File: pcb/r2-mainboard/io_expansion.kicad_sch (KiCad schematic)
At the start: 6 parts, among them J22 HC-FPC-05-09-6RLTAG, J23 HC-FPC-05-09-6RLTAG, U54 TPS22914BYFPR, U55 TPS22914BYFPR

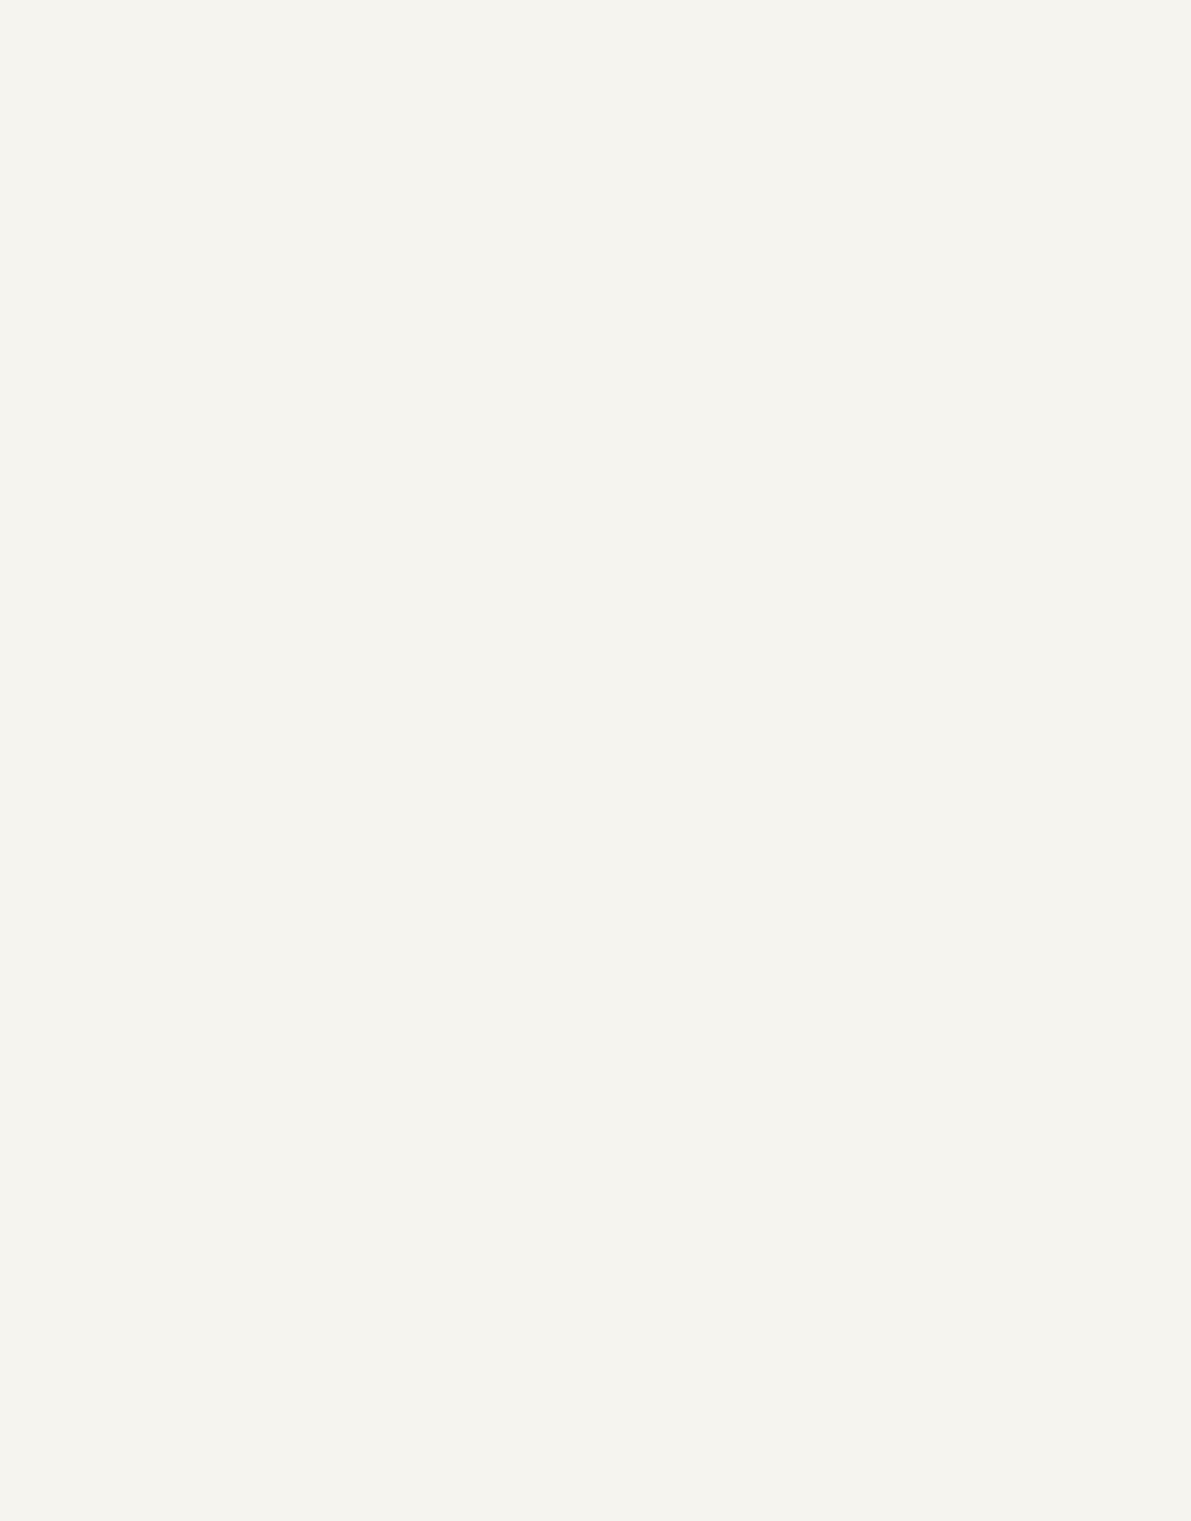
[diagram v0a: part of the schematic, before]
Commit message: change layout and reduce board size + add second usb host only
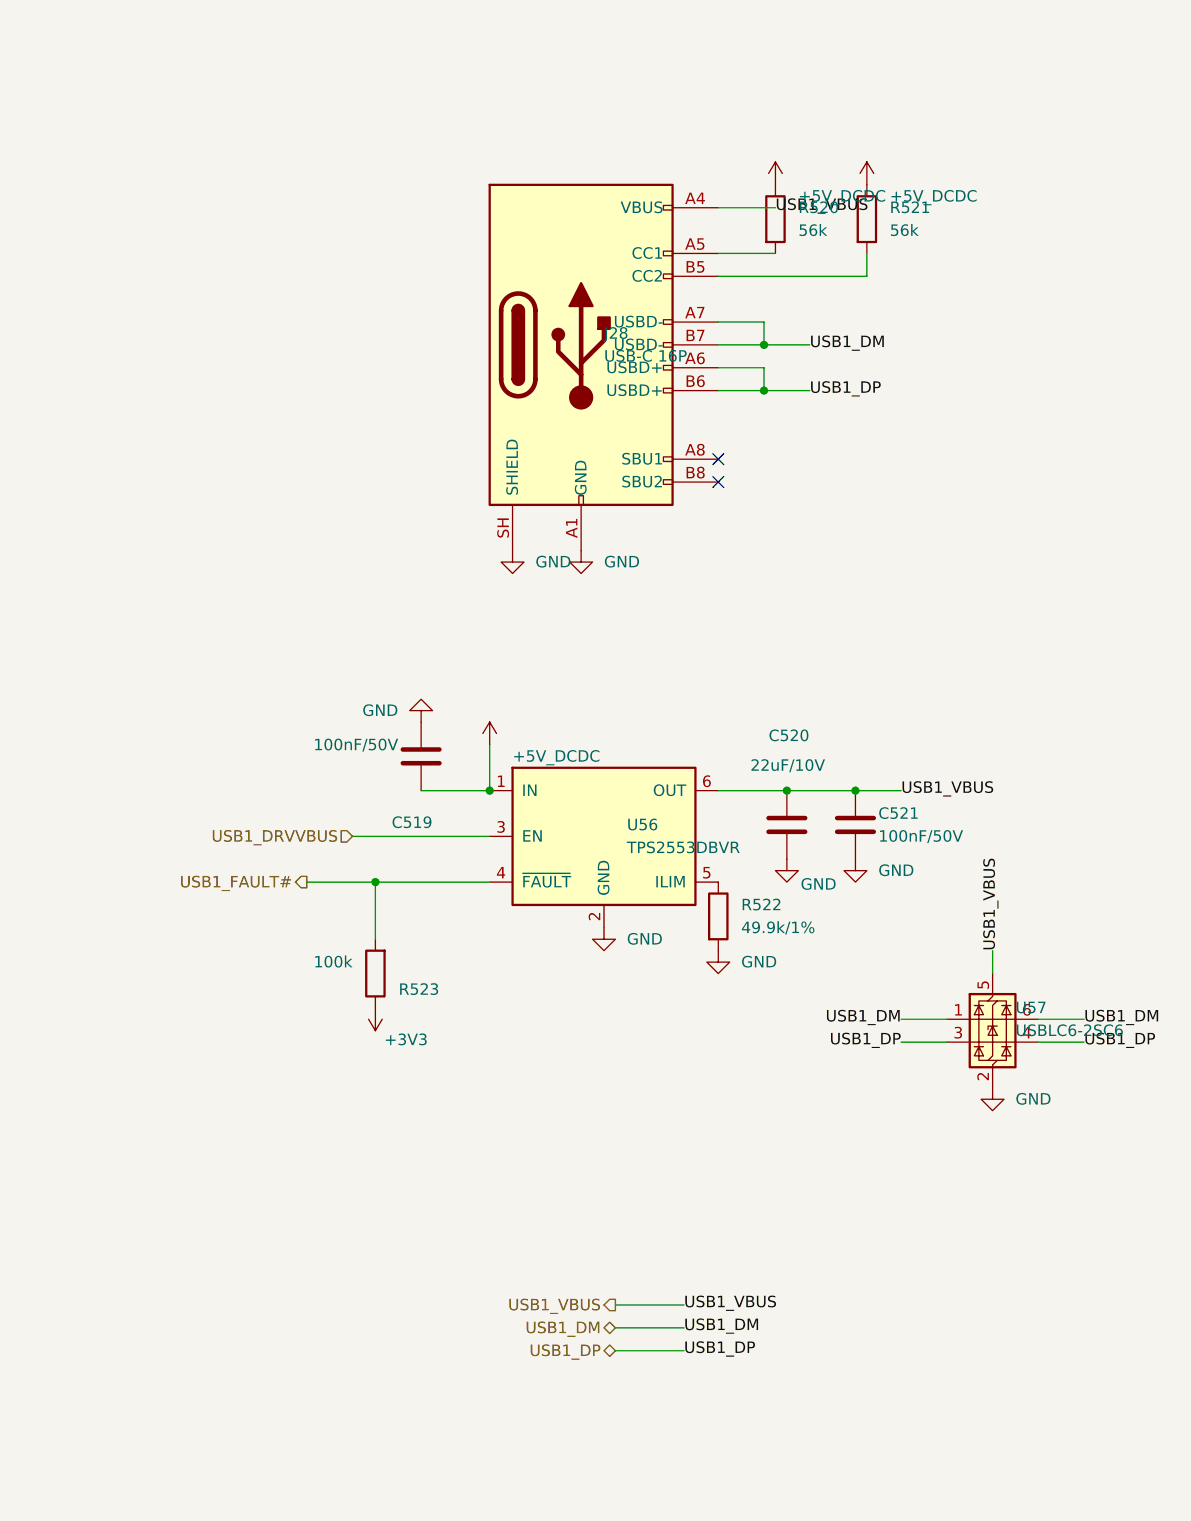
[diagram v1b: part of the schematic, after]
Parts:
- added C519, C521: 100nF/50V, Capacitor_SMD:C_0402_1005Metric, symbol Device:C
- added C520: 22uF/10V, Capacitor_SMD:C_0805_2012Metric, symbol Device:C
- added J28: USB-C 16P, Connector_USB:USB_C_Receptacle_HRO_TYPE-C-31-M-12, symbol Connector:USB_C_Receptacle_USB2.0_16P
- added R520, R521: 56k, Resistor_SMD:R_0402_1005Metric, symbol Device:R
- added R522: 49.9k/1%, Resistor_SMD:R_0402_1005Metric, symbol Device:R
- added R523: 100k, Resistor_SMD:R_0402_1005Metric, symbol Device:R
- added U56: TPS2553DBVR, Package_TO_SOT_SMD:SOT-23-6, symbol r2:TPS2553DBV
- added U57: USBLC6-2SC6, Package_TO_SOT_SMD:SOT-23-6, symbol r2:USBLC6-2SC6
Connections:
- net +3V3: now also R523.1
- net GND: now also C519.2, C520.2, C521.2, J28.A1 (GND), J28.A12 (GND), J28.B1 (GND), J28.B12 (GND), J28.SH (SHIELD), R522.2, U56.2 (GND), U57.2 (GND)
- new net: R522.1, U56.5 (ILIM)
- new net: J28.A5 (CC1), R520.2
- new net: J28.B5 (CC2), R521.2
- new net +5V_DCDC: C519.1, R520.1, R521.1, U56.1 (IN)
- new net USB1_DM: J28.A7 (USBD-), J28.B7 (USBD-), U57.1 (I/O1), U57.6 (I/O1)
- new net USB1_DP: J28.A6 (USBD+), J28.B6 (USBD+), U57.3 (I/O2), U57.4 (I/O2)
- new net USB1_DRVVBUS: U56.3 (EN)
- new net USB1_FAULT#: R523.2, U56.4 (~{FAULT})
- new net USB1_VBUS: C520.1, C521.1, J28.A4 (VBUS), J28.A9 (VBUS), J28.B4 (VBUS), J28.B9 (VBUS), U56.6 (OUT), U57.5 (VBUS)
- no-connect marks 0 -> 2
